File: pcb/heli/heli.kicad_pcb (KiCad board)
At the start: 4 copper layers, 50.6 x 50 mm, 74 parts, among them J1 Batterie, J2 Debug, J3 CONMHF4-SMD-G-T, J4 Servo, J5 Servo, M1 Motor_DC, M2 Motor_DC, Q1 IRLZ44N, Q2 BC547, Q3 IRLZ44N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

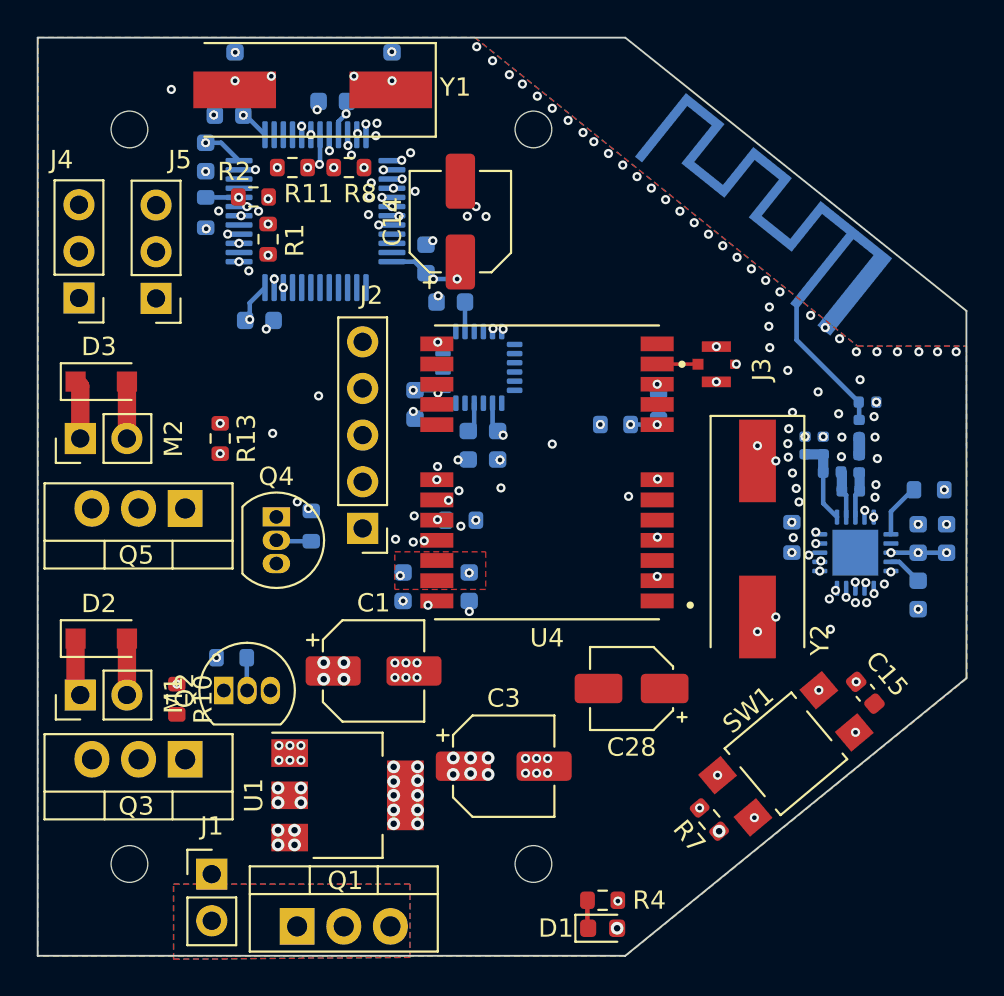
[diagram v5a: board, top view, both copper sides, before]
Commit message: 
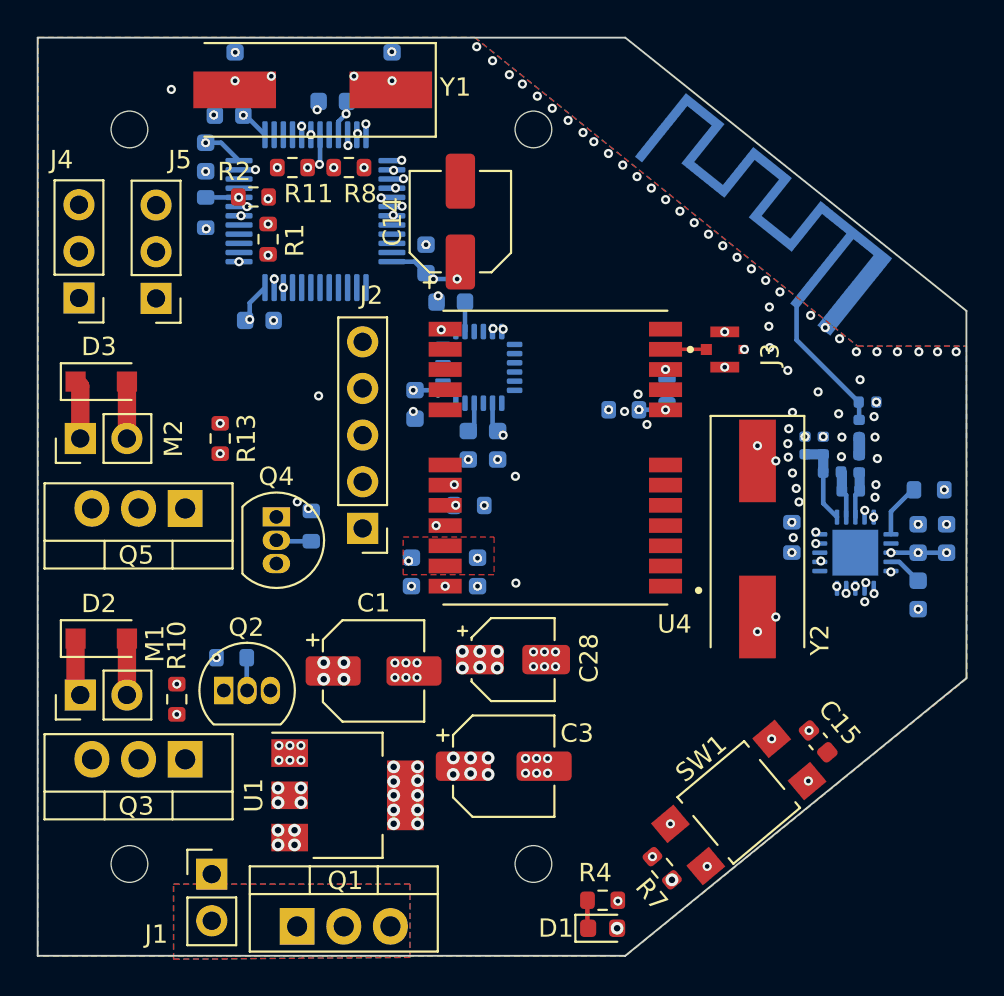
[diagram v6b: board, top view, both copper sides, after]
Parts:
- moved C28 6.64 mm to (43.9, 48.9), turned to 0 degrees
- moved C15 3.69 mm to (60.5, 53.3)
- moved R7 3.69 mm to (52.0, 60.2)
- moved SW1 3.69 mm to (56.2, 56.7)
- moved R14 0.92 mm to (41.5, 40.5)
- moved C27 0.92 mm to (52.3, 34.2)
- moved C25 0.92 mm to (38.4, 44.1)
- moved C26 0.92 mm to (42.0, 44.1)
- moved R15 0.92 mm to (49.9, 35.3)
- moved U4 0.92 mm to (46.2, 37.9)
- moved J3 0.92 mm to (55.4, 32.0)
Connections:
- U3 pad 39: GPS_IRQ -> unconnected-(U3-Pad39)
- U4 pad 4: GPS_IRQ -> unconnected-(U4-Pad4)
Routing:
- net RADIO_IRQ: track 46.1 -> 0.00 mm, vias 4 -> 0
- net GPS_IRQ: track 33.5 -> 0.00 mm, vias 5 -> 0
- net RESET: track 60.7 -> 27.9 mm, vias 7 -> 6
- net GPS_CSN: track 21.8 -> 0.00 mm, vias 3 -> 0
- net RADIO_CSN: track 43.3 -> 60.4 mm
- net SPI_SCK: track 43.0 -> 59.0 mm, vias 3 -> 5
- net RADIO_CE: track 45.1 -> 56.8 mm, vias 4 -> 3
- net SPI_MISO: track 42.3 -> 52.8 mm
- net Net-(Q2-Pad1): track 0.46 -> 7.25 mm, vias 0 -> 1
- net SPI_MOSI: track 44.6 -> 49.6 mm
- net GPS_NRST: track 24.4 -> 26.4 mm
- net GND: track 0.04 -> 0.00 mm, vias 139 -> 120
- net 3.3V: vias 44 -> 50

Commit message: 
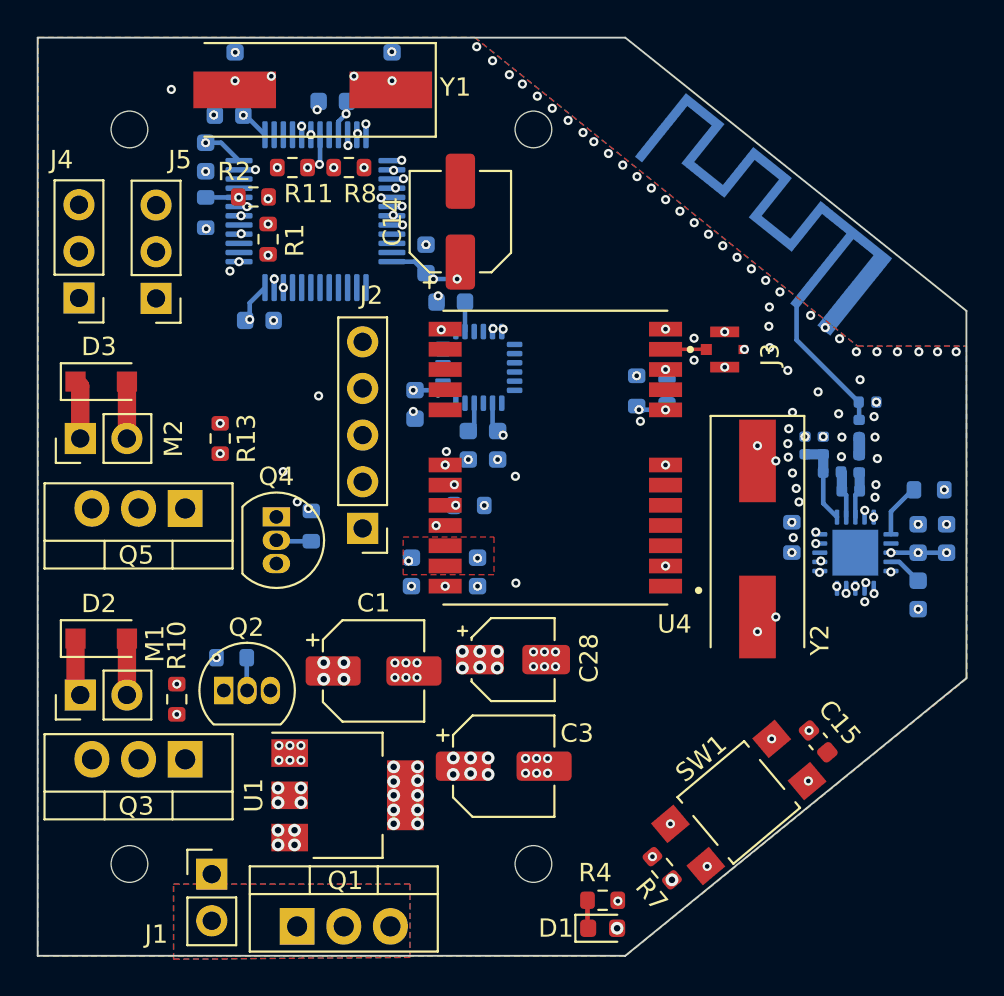
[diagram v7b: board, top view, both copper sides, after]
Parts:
- moved R15 1.24 mm to (50.6, 34.2), turned to -90 degrees
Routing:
- net RESET: track 27.9 -> 63.4 mm, vias 6 -> 7
- net RADIO_IRQ: track 0.00 -> 32.8 mm, vias 0 -> 2
- net GPS_CSN: track 0.00 -> 20.8 mm, vias 0 -> 3
- net RADIO_CSN: track 60.4 -> 62.8 mm
- net Net-(Q2-Pad1): track 7.25 -> 6.61 mm
- net 3.3V: track 17.5 -> 17.0 mm
- net RADIO_CE: track 56.8 -> 57.1 mm, vias 3 -> 4
- net SWCLK: vias 1 -> 2
- net GND: vias 120 -> 126

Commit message: 
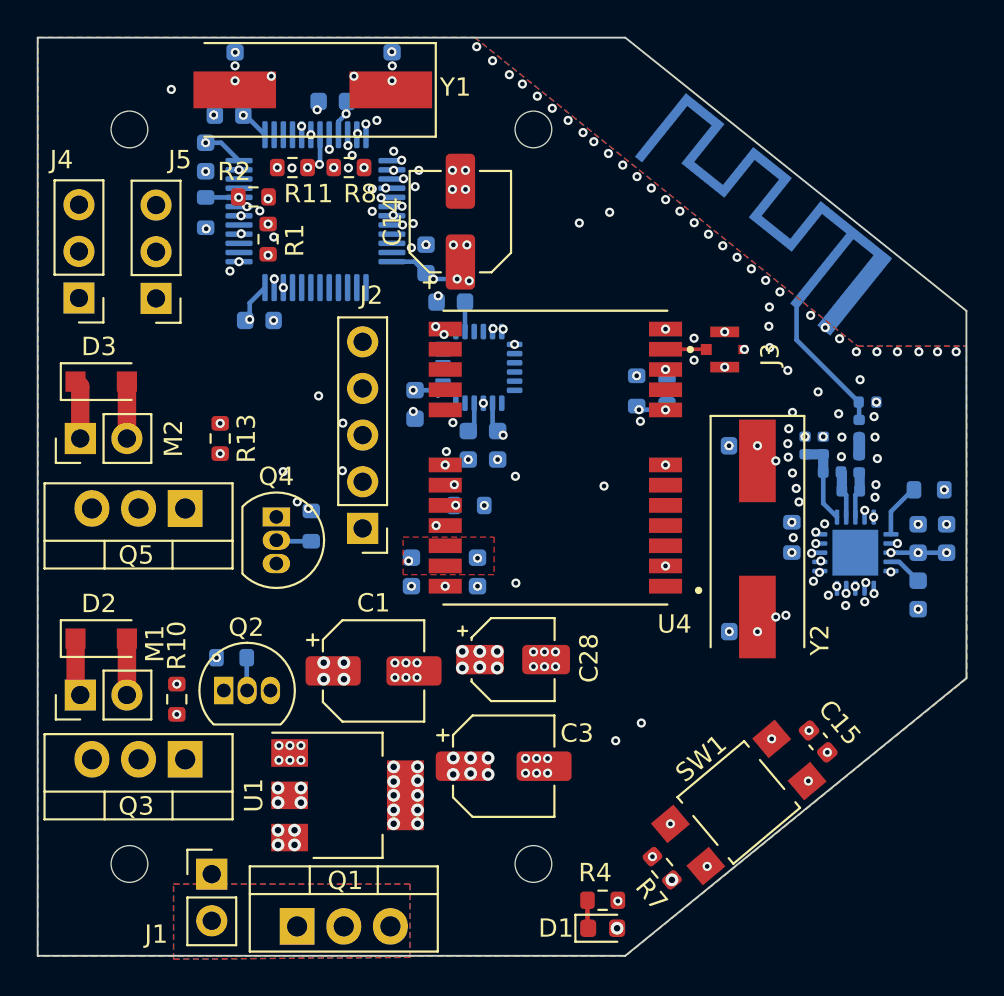
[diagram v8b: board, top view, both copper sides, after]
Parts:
- moved C20 1.10 mm to (56.4, 37.2), turned to 180 degrees
- moved C17 1.08 mm to (56.4, 47.3), turned to 180 degrees
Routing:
- net SPI_MISO: track 52.8 -> 53.4 mm
- net GND: vias 126 -> 167
- net 3.3V: vias 50 -> 53
